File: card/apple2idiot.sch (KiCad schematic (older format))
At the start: 4 parts, among them J1 CARD EDGE, U1 IDT7132, U2 ESP32-WROOM-32

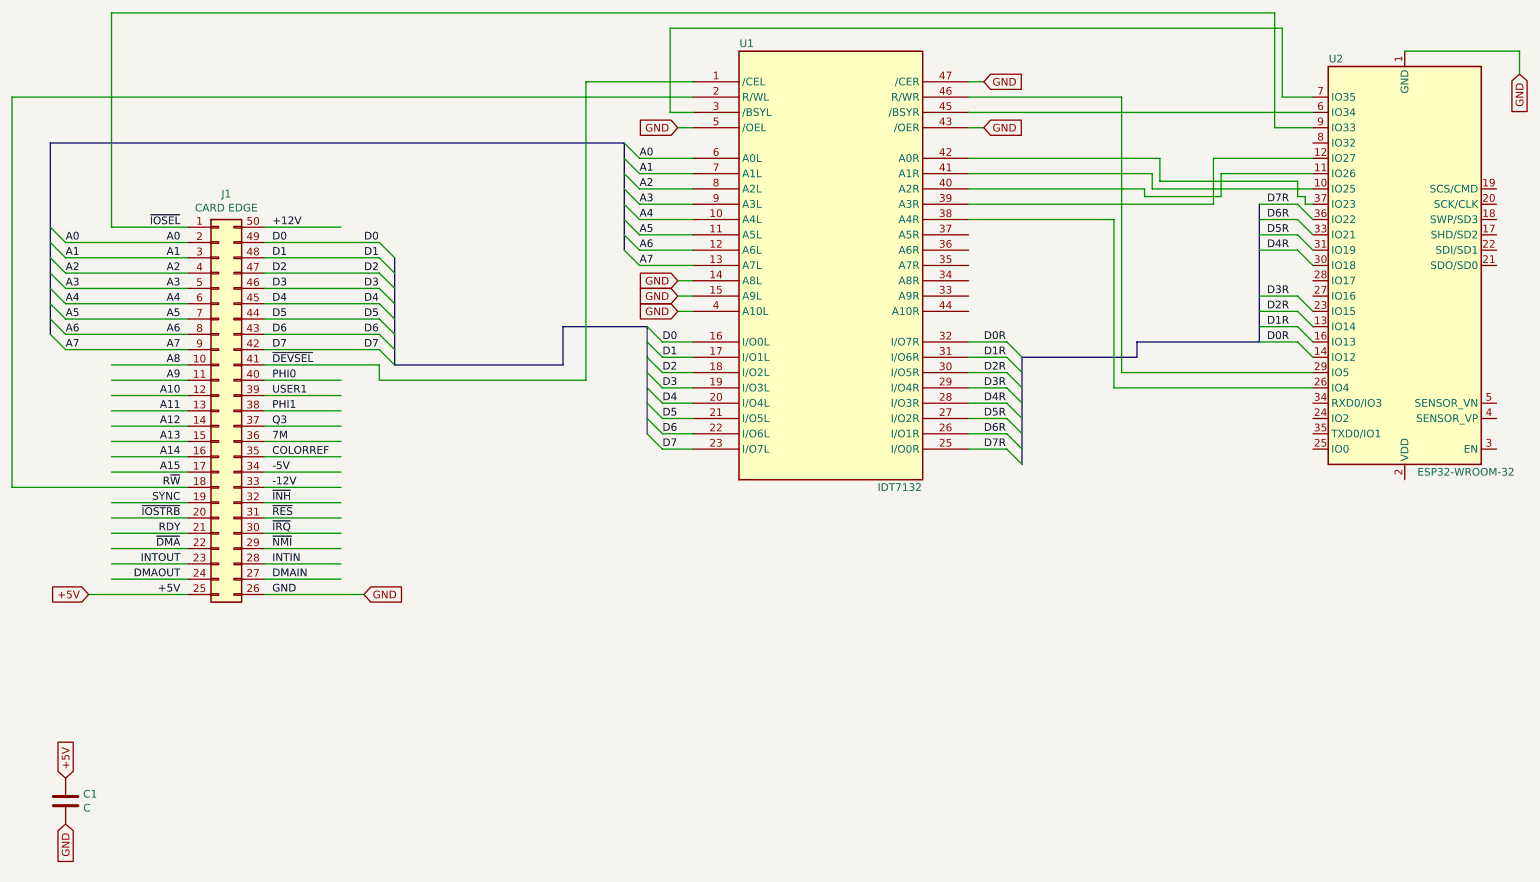
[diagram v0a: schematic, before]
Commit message: ESP w/ webserver writes to RAM
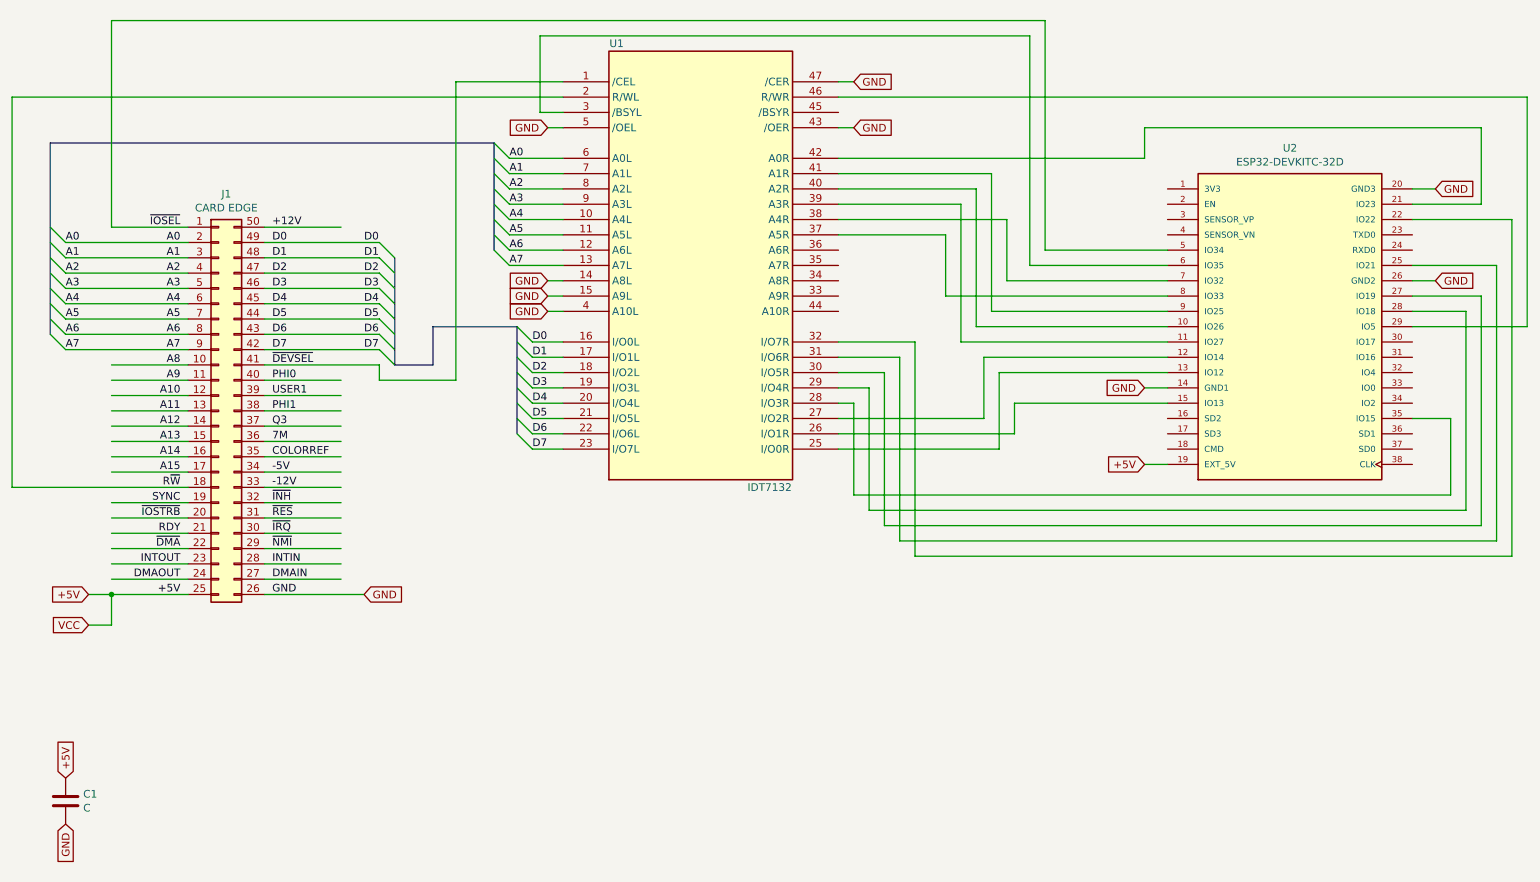
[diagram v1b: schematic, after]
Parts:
- removed U2: ESP32-WROOM-32, RF_Module:ESP32-WROOM-32, symbol RF_Module:ESP32-WROOM-32
- added U2: ESP32-DEVKITC-32D, ESPDEVKIT:MODULE_ESP32-DEVKITC-32D, symbol ESP32-DEV_KIT:ESP32-DEVKITC-32D
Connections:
- net labels added: VCC
- net labels removed: D0R, D1R, D2R, D3R, D4R, D5R, D6R, D7R
- wire segments 130 -> 151
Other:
- moved on the sheet: U1

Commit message: going to silver city
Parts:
- added JP? (x4): Jumper_3_Bridged12, symbol Jumper:Jumper_3_Bridged12
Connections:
- wire segments 151 -> 158
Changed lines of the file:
@@
 GND
-Wire Wire Line
-	4250 1350 4100 1350
 Wire Wire Line
 	4250 2450 4150 2450
@@
 Wire Wire Line
 	3900 1650 4250 1650
-$Comp
-L Memory_RAM:IDT7132 U1
-U 1 1 6102DC5C
-P 5150 2350
-F 0 "U1" H 4600 3800 50  0000 C CNN
-F 1 "IDT7132" H 5600 900 50  0000 C CNN
-F 2 "Package_DIP:DIP-48_W15.24mm_Socket_LongPads" H 5150 2350 50  0001 C CNN
-F 3 "" H 5150 2350 50  0001 C CNN
-	1    5150 2350
-	1    0    0    -1
-$EndComp
 Entry Wire Line
 	3800 1550 3900 1650
@@
 	6250 3950 10150 3950
 Wire Wire Line
-	10150 3950 10150 2650
-Wire Wire Line
-	10150 2650 9800 2650
-Wire Wire Line
 	6050 3050 6350 3050
 Wire Wire Line
@@
 	6350 4050 10250 4050
 Wire Wire Line
-	10250 4050 10250 2550
-Wire Wire Line
-	10250 2550 9800 2550
-Wire Wire Line
 	6050 2950 6450 2950
 Wire Wire Line
@@
 Wire Wire Line
 	6450 4150 10350 4150
-Wire Wire Line
-	10350 4150 10350 2350
-Wire Wire Line
-	10350 2350 9800 2350
 Text GLabel 9950 2450 2    50   Input ~ 0
 GND
@@
 	6550 4250 10450 4250
 Wire Wire Line
-	10450 4250 10450 2050
-Wire Wire Line
-	10450 2050 9800 2050
-Wire Wire Line
-	6050 1650 8050 1650
-Wire Wire Line
-	8050 1650 8050 1450
-Wire Wire Line
-	8050 1450 10250 1450
-Wire Wire Line
-	10250 1450 10250 1950
-Wire Wire Line
-	10250 1950 9800 1950
-Wire Wire Line
-	6050 1750 7050 1750
-Wire Wire Line
-	7050 1750 7050 2650
-Wire Wire Line
-	7050 2650 8200 2650
-Wire Wire Line
-	6050 1850 6950 1850
-Wire Wire Line
-	6950 1850 6950 2750
-Wire Wire Line
-	6950 2750 8200 2750
-Wire Wire Line
-	6050 1950 6850 1950
-Wire Wire Line
-	6850 1950 6850 2850
-Wire Wire Line
-	6850 2850 8200 2850
-Wire Wire Line
-	4100 850  7300 850
-Wire Wire Line
-	7300 850  7300 2350
-Wire Wire Line
-	7300 2350 8200 2350
-Wire Wire Line
-	4100 850  4100 1350
-Wire Wire Line
 	1300 750  7400 750
 Wire Wire Line
-	7400 750  7400 2250
-Wire Wire Line
-	7400 2250 8200 2250
-Wire Wire Line
 	1300 750  1300 2100
-Wire Wire Line
-	6050 2050 7150 2050
-Wire Wire Line
-	6050 2150 6750 2150
-Wire Wire Line
-	6750 2150 6750 2550
-Wire Wire Line
-	6750 2550 8200 2550
-Wire Wire Line
-	7150 2050 7150 2450
-Wire Wire Line
-	7150 2450 8200 2450
 Wire Wire Line
 	6050 1250 10550 1250
@@
 Wire Wire Line
 	1300 4700 1300 4500
+Connection ~ 1300 4500
+Wire Wire Line
+	1300 4500 1800 4500
+Wire Wire Line
+	10150 3950 10150 2950
+Wire Wire Line
+	10150 2950 9800 2950
+Wire Wire Line
+	10250 4050 10250 2850
+Wire Wire Line
+	10250 2850 9800 2850
+Wire Wire Line
+	10350 4150 10350 2650
+Wire Wire Line
+	10350 2650 9800 2650
+Wire Wire Line
+	10450 4250 10450 2550
+Wire Wire Line
+	10450 2550 9800 2550
+Wire Wire Line
+	6050 1350 7550 1350
+Wire Wire Line
+	7550 1350 7550 2050
+Wire Wire Line
+	7550 2050 8200 2050
+Wire Wire Line
+	6050 1650 7750 1650
+$Comp
+L Jumper:Jumper_3_Bridged12 JP?
+U 1 1 61177187
+P 7950 950
+F 0 "JP?" H 7950 1154 50  0000 C CNN
+F 1 "Jumper_3_Bridged12" H 7950 1063 50  0000 C CNN
+F 2 "" H 7950 950 50  0001 C CNN
+F 3 "~" H 7950 950 50  0001 C CNN
+	1    7950 950
+	1    0    0    -1
+$EndComp
+$Comp
+L Memory_RAM:IDT7132 U1
+U 1 1 6102DC5C
+P 5150 2350
+F 0 "U1" H 4600 3800 50  0000 C CNN
+F 1 "IDT7132" H 5600 900 50  0000 C CNN
+F 2 "Package_DIP:DIP-48_W15.24mm_Socket_LongPads" H 5150 2350 50  0001 C CNN
+F 3 "" H 5150 2350 50  0001 C CNN
+	1    5150 2350
+	1    0    0    -1
+$EndComp
+Wire Wire Line
+	7400 750  7400 950
+Wire Wire Line
+	7400 950  7700 950
+Wire Wire Line
+	7950 1100 7950 2250
+Wire Wire Line
+	7950 2250 8200 2250
+$Comp
+L Jumper:Jumper_3_Bridged12 JP?
+U 1 1 61190E6D
+P 4450 5250
+F 0 "JP?" H 4450 5454 50  0000 C CNN
+F 1 "Jumper_3_Bridged12" H 4450 5363 50  0000 C CNN
+F 2 "" H 4450 5250 50  0001 C CNN
+F 3 "~" H 4450 5250 50  0001 C CNN
+	1    4450 5250
+	1    0    0    -1
+$EndComp
+Wire Wire Line
+	4250 1350 3700 1350
+Wire Wire Line
+	3700 1350 3700 5250
+Wire Wire Line
+	3700 5250 4200 5250
+$Comp
+L Jumper:Jumper_3_Bridged12 JP?
+U 1 1 611B120A
+P 6200 5250
+F 0 "JP?" H 6200 5361 50  0000 C CNN
+F 1 "Jumper_3_Bridged12" H 6200 5452 50  0000 C CNN
+F 2 "" H 6200 5250 50  0001 C CNN
+F 3 "~" H 6200 5250 50  0001 C CNN
+	1    6200 5250
+	-1   0    0    1
+$EndComp
+$Comp
+L Jumper:Jumper_3_Bridged12 JP?
+U 1 1 61193046
+P 5350 5250
+F 0 "JP?" H 5350 5454 50  0000 C CNN
+F 1 "Jumper_3_Bridged12" H 5350 5363 50  0000 C CNN
+F 2 "" H 5350 5250 50  0001 C CNN
+F 3 "~" H 5350 5250 50  0001 C CNN
+	1    5350 5250
+	-1   0    0    1
+$EndComp
+Wire Wire Line
+	7750 1350 10500 1350
+Wire Wire Line
+	10500 1350 10500 2350
+Wire Wire Line
+	10500 2350 9800 2350
+Wire Wire Line
+	7750 1350 7750 1650
+Wire Wire Line
+	6050 1750 7850 1750
+Wire Wire Line
+	7850 1750 7850 1450
+Wire Wire Line
+	7850 1450 10400 1450
+Wire Wire Line
+	10400 1450 10400 2050
+Wire Wire Line
+	9800 2050 10400 2050
+Wire Wire Line
+	6050 1850 8050 1850
+Wire Wire Line
+	8050 1850 8050 1550
+Wire Wire Line
+	8050 1550 10300 1550
+Wire Wire Line
+	10300 1550 10300 1950
+Wire Wire Line
+	9800 1950 10300 1950
+Wire Wire Line
+	6050 1950 7350 1950
+Wire Wire Line
+	7350 1950 7350 2650
+Wire Wire Line
+	7350 2650 8200 2650
+Wire Wire Line
+	6050 2050 7250 2050
+Wire Wire Line
+	7250 2050 7250 2750
+Wire Wire Line
+	7250 2750 8200 2750
+Wire Wire Line
+	6050 2150 7100 2150
+Wire Wire Line
+	7100 2150 7100 2850
+Wire Wire Line
+	7100 2850 8200 2850
 Wire Bus Line
 	3150 2300 3150 3000
@@
 Wire Bus Line
 	900  1550 900  2800
-Connection ~ 1300 4500
-Wire Wire Line
-	1300 4500 1800 4500
 $EndSCHEMATC
